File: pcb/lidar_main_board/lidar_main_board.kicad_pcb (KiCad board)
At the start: 2 copper layers, 70 x 50 mm, 27 parts, among them J1 vl53l1x, J2 AS5600, J3 HC-06, J4 Bateria, J5 Boton 1, J6 Boton 2, J7 Boton 3, J8 Motor, U1 LPC845-BRK, U2 AMS1117-3.3, U3 LM7805_TO220

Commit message: new version pcb
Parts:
- added D3: LED, LED_THT:LED_D5.0mm, F.Cu at (79.2, 22.3)
- added R5: 120, Resistor_THT:R_Axial_DIN0207_L6.3mm_D2.5mm_P10.16mm_Horizontal, F.Cu at (75.6, 34.2)
- D1: value LED_PWR -> LED
- J2: footprint Connector_PinHeader_2.54mm:PinHeader_1x04_P2.54mm_Vertical -> Connector_PinHeader_2.54mm:PinHeader_1x05_P2.54mm_Vertical
- moved D2 64.3 mm to (23.1, 56.6)
- moved R4 53.3 mm to (29.4, 55.2), turned to 0 degrees
- moved D1 34.6 mm to (56.5, 53.1), turned to 90 degrees
- moved R2 21.2 mm to (85.7, 38.5)
- moved R3 16.4 mm to (75.6, 42.9), turned to 0 degrees
- moved C1 13.5 mm to (51.6, 58.1), turned to 0 degrees
- moved R1 10.6 mm to (72.9, 50.6), turned to 180 degrees
- moved J3 8.32 mm to (65.4, 27.2)
- moved C2 6.52 mm to (62.3, 57.8)
- moved J6 5.86 mm to (35.4, 22.1)
- moved J7 4.42 mm to (30.2, 22.1)
- moved J2 2.80 mm to (61.4, 27.2)
- moved U2 2.56 mm to (57.7, 65.3)
- moved C3 1.29 mm to (78.9, 64.5)
- moved C5 1.25 mm to (65.6, 60.4)
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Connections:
- A1 pad 12: GND -> MS3
- A1 pad 13: +3V3 -> MRESET
- A1 pad 14: +3V3 -> MSLEEP
- D2 pad 1: LED_DIR -> GND
- J4 pad 1: GND -> +BATT
- J4 pad 2: +BATT -> GND
- R4 pad 1: +3V3 -> DIR
- U1 pad 12: unconnected-(U1-PIO0_26-Pad12) -> DIR_AS5600
- U1 pad 16: BTN_SEL -> BTN_MODE
- U1 pad 17: BTN_MODE -> BTN_SEL
- U1 pad 22: unconnected-(U1-PIO0_09-Pad22) -> DIR
- U1 pad 23: DIR -> STEP
- U1 pad 24: STEP -> MSLEEP
- U1 pad 26: unconnected-(U1-PIO0_13-Pad26) -> MRESET
- U1 pad 27: unconnected-(U1-PIO0_14-Pad27) -> MS3
- U1 pad 36: LED_DIR -> unconnected-(U1-PIO0_03_SWCLK-Pad36)
- U1 pad 6: unconnected-(U1-PIO0_21-Pad6) -> I2C1 - SCL
- U1 pad 7: I2C1 - SCL -> I2C1 - SDA
- U1 pad 8: I2C1 - SDA -> unconnected-(U1-PIO0_23-Pad8)
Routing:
- net GND: track 201.3 -> 289.3 mm
- net STEP: track 4.37 -> 57.5 mm
- net +3V3: track 221.0 -> 168.5 mm, vias 2 -> 0
- net LED_DIR: track 35.4 -> 0.00 mm
- net +5V: track 122.8 -> 100.0 mm
- net BAT_ADC: track 12.6 -> 29.6 mm
- net Net-(D3-A): track 0.00 -> 12.1 mm
- net +BATT: track 35.6 -> 46.1 mm
- net UART0 - RX: track 13.8 -> 4.15 mm
- net Net-(D2-A): track 7.01 -> 16.7 mm
- net DIR: track 4.37 -> 13.9 mm
- net DIR_AS5600: track 0.00 -> 9.24 mm
- net UART0 - TX: track 13.2 -> 4.15 mm
- net MSLEEP: track 0.00 -> 5.66 mm
- net MS3: track 0.00 -> 4.06 mm
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
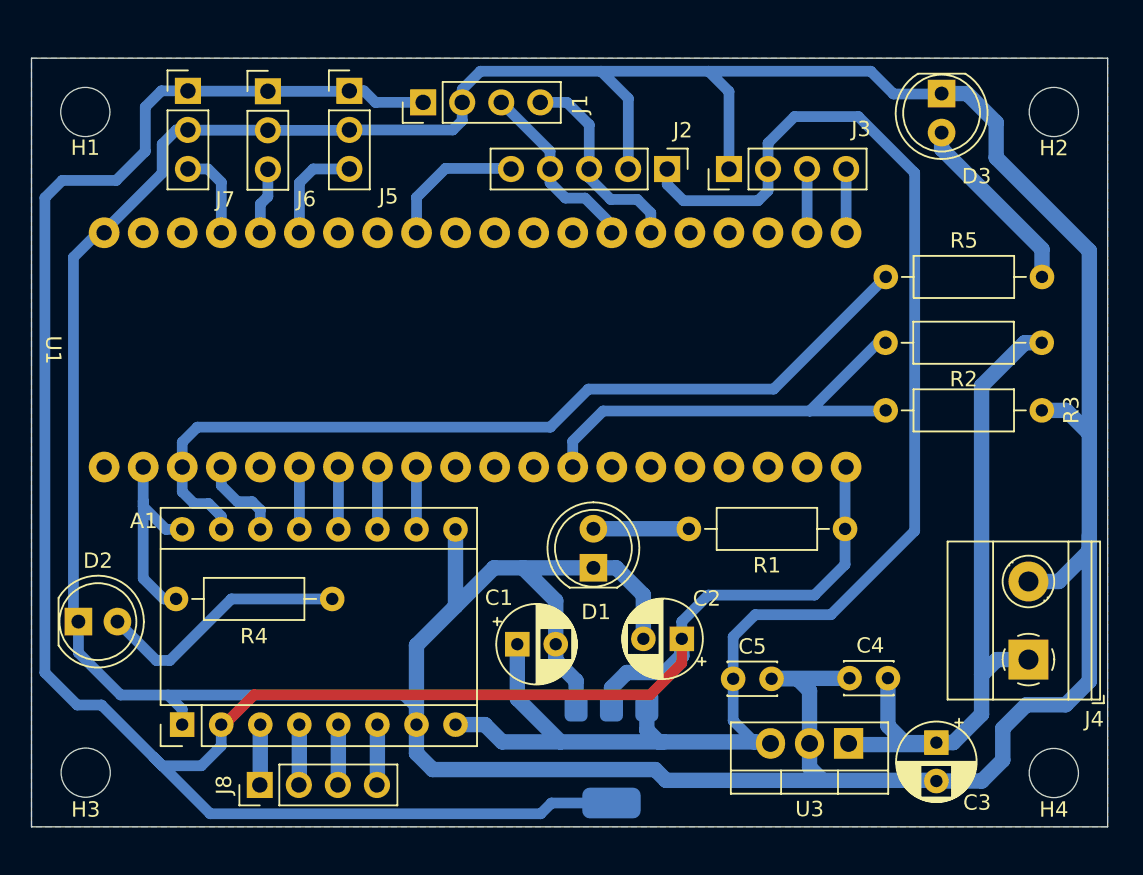
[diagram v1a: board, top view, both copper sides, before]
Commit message: molex in pcb
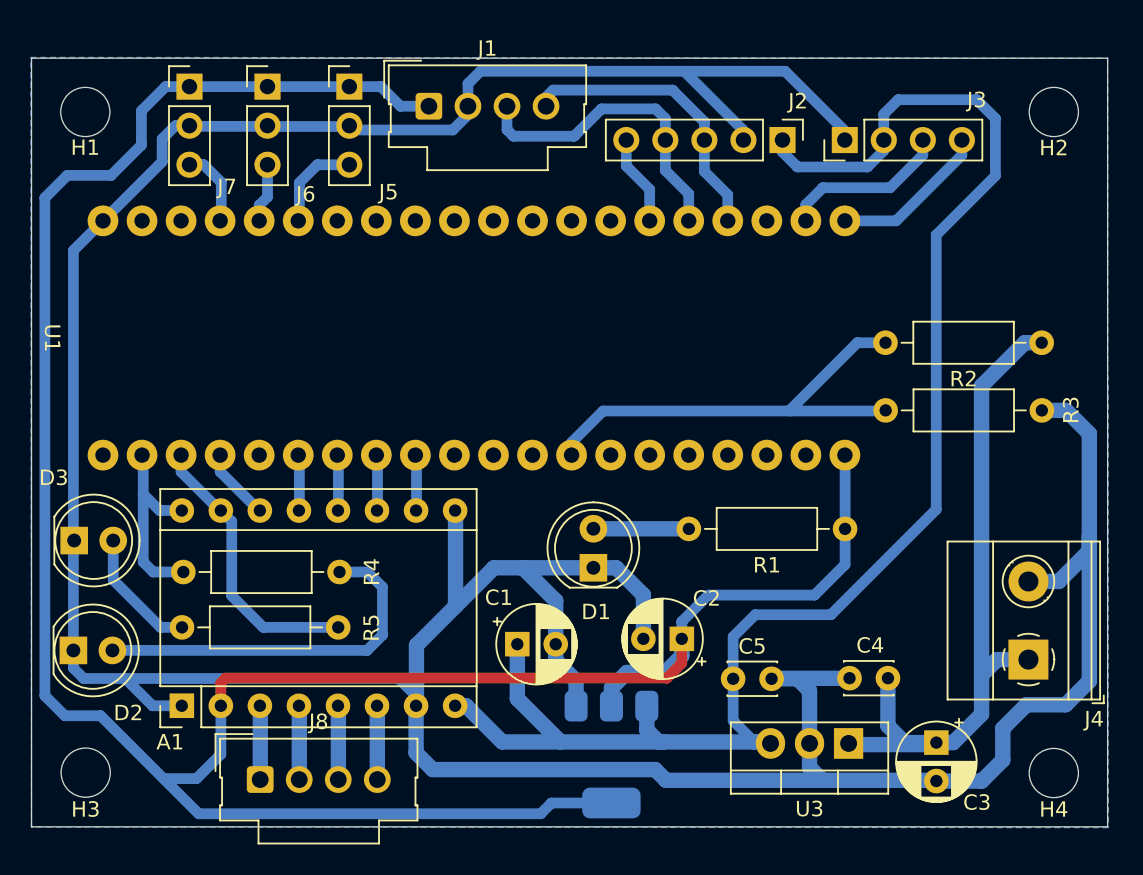
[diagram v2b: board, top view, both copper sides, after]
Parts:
- J1, J8: footprint Connector_PinHeader_2.54mm:PinHeader_1x04_P2.54mm_Vertical -> Connector_Molex:Molex_SL_171971-0004_1x04_P2.54mm_Vertical
- moved D3 63.5 mm to (22.8, 51.4), turned to 0 degrees
- moved R5 42.3 mm to (40.0, 57.0), turned to 180 degrees
- moved J3 7.76 mm to (72.9, 25.3)
- moved J2 7.73 mm to (68.8, 25.3)
- moved D2 1.90 mm to (22.7, 58.5)
- moved R4 1.81 mm to (29.9, 53.4)
- moved A1 1.23 mm to (29.8, 62.1)
- moved U1 0.78 mm to (56.4, 38.2)
- moved J1 0.45 mm to (45.9, 23.1), turned to 0 degrees
- moved J8 0.35 mm to (34.9, 66.9), turned to 0 degrees
- moved J6 0.30 mm to (35.4, 21.9)
- moved J7 0.29 mm to (30.3, 21.9)
- moved J5 0.27 mm to (40.7, 21.9)
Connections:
- U1 pad 12: DIR_AS5600 -> unconnected-(U1-PIO0_26-Pad12)
- U1 pad 4: unconnected-(U1-PIO0_19-Pad4) -> I2C1 - SCL
- U1 pad 5: unconnected-(U1-PIO0_20-Pad5) -> I2C1 - SDA
- U1 pad 6: I2C1 - SCL -> DIR_AS5600
- U1 pad 7: I2C1 - SDA -> unconnected-(U1-PIO0_22-Pad7)
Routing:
- net STEP: track 57.5 -> 18.3 mm
- net GND: track 289.3 -> 253.1 mm
- net I2C1 - SDA: track 12.2 -> 20.5 mm
- net Net-(D2-A): track 16.7 -> 24.3 mm
- net UART0 - RX: track 4.15 -> 11.0 mm
- net UART0 - TX: track 4.15 -> 10.4 mm
- net I2C1 - SCL: track 13.5 -> 19.0 mm
- net Net-(D3-A): track 12.1 -> 8.32 mm
- net DIR_AS5600: track 9.24 -> 5.88 mm
- net +3V3: track 168.5 -> 171.8 mm
- net +5V: track 100.0 -> 101.8 mm
- net DIR: track 13.9 -> 12.8 mm
- net MSLEEP: track 5.66 -> 4.79 mm
- net Net-(A1-1B): track 3.94 -> 4.81 mm
- net Net-(A1-2A): track 3.94 -> 4.81 mm
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
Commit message: feat: pcb desing used
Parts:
- R2: value 33k -> 100k
- R3: value 20k -> 62k
- moved J7 0.12 mm to (30.1, 21.9)
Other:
- board text added: "Pablo Gomez 4-12 UTN FRA 2024"
